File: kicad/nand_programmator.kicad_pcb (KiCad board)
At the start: 2 copper layers, 48 x 41 mm, 42 parts, among them J1 Conn_01x04, J2 Conn_01x03, J3 Conn_02x12_Odd_Even_Left, J4 Conn_02x12_Odd_Even_Right, J5 BOOT0, J6 ~{RST}, P1 USB, U1 LM1117-3.3, U2 STM32F103VCT6, Y1 Crystal_SMD_8MHz_18pF

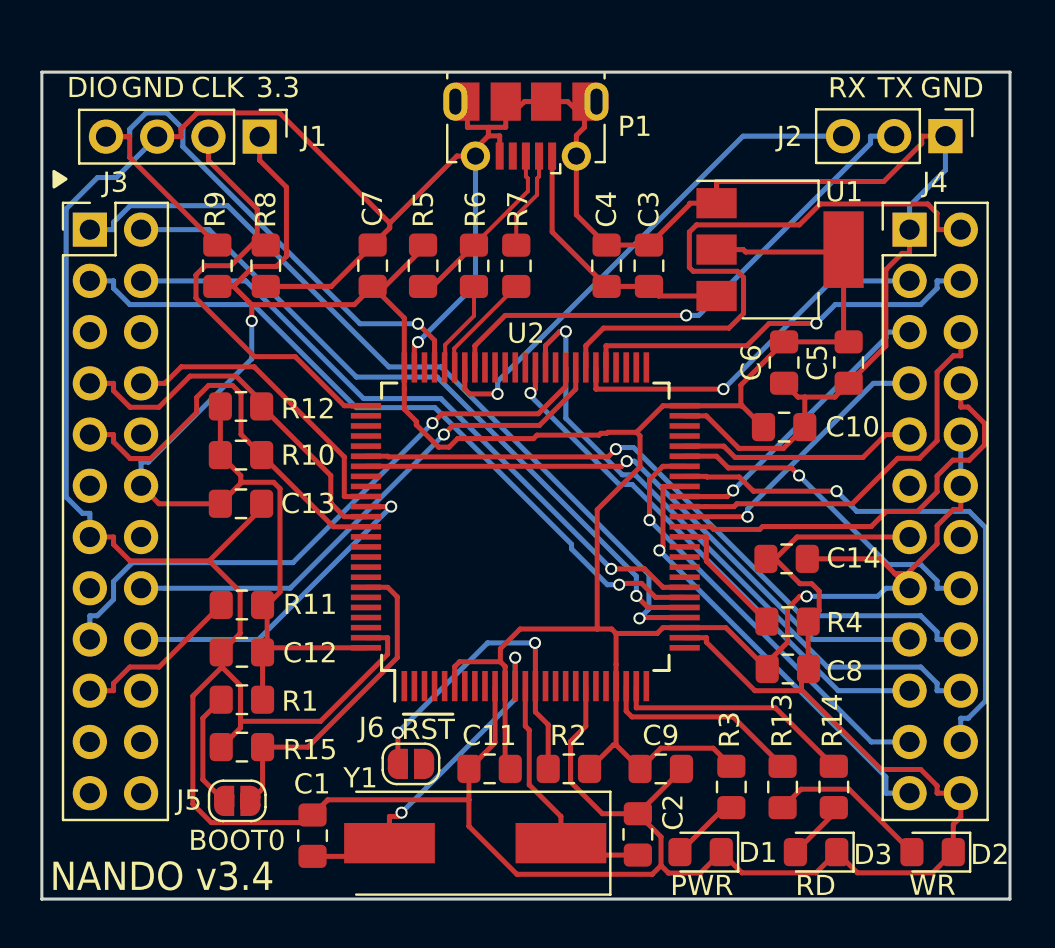
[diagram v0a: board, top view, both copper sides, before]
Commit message: Migrate mainboard and adapter_tsop48 to kicad 10 and various changes
Replace the regulator with an AMS1117-3.3 and change the USB port to a generic USB-C port.
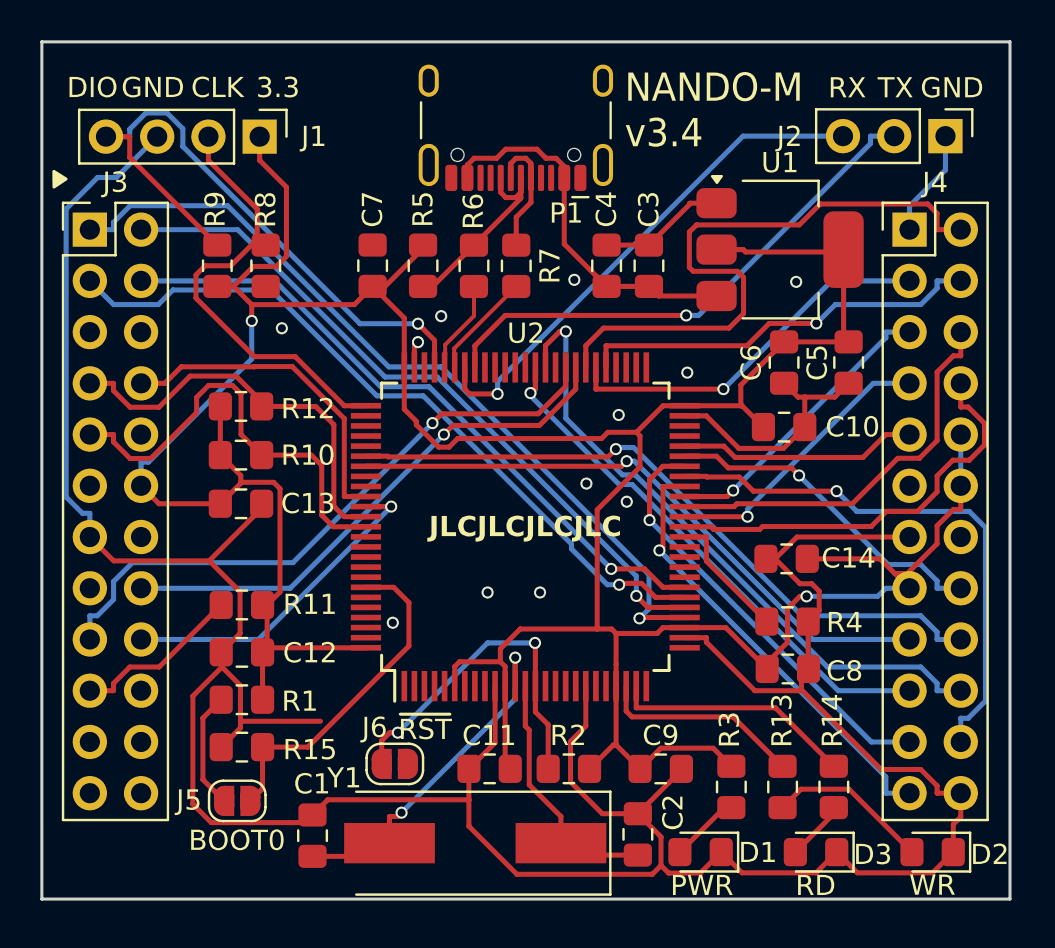
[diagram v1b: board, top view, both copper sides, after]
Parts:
- P1: value USB -> USB_C_Receptacle_USB2.0_16P; footprint lib_fp:USB_Micro-B_Molex-105017-0001 -> Connector_USB:USB_C_Receptacle_HCTL_HC-TYPE-C-16P-01A
- U1: value LM1117-3.3 -> AMS1117-3.3; footprint lib_fp:SOT-223 -> Package_TO_SOT_SMD:SOT-223-3_TabPin2
- Y1: value Crystal_SMD_8MHz_18pF -> 8MHz 18pF
- moved P1 1.30 mm to (191.4, 46.1)
- moved J6 0.80 mm to (185.4, 78.9)
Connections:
- J3 pad 10: Net-(J3-Pad10) -> unconnected-(J3-Pin_10-Pad10)
- J3 pad 11: Net-(J3-Pad11) -> unconnected-(J3-Pin_11-Pad11)
- J3 pad 14: Net-(J3-Pad14) -> unconnected-(J3-Pin_14-Pad14)
- J3 pad 15: Net-(J3-Pad15) -> unconnected-(J3-Pin_15-Pad15)
- J3 pad 20: Net-(J3-Pad20) -> unconnected-(J3-Pin_20-Pad20)
- J3 pad 21: Net-(J3-Pad21) -> unconnected-(J3-Pin_21-Pad21)
- J3 pad 22: Net-(J3-Pad22) -> unconnected-(J3-Pin_22-Pad22)
- J3 pad 23: Net-(J3-Pad23) -> unconnected-(J3-Pin_23-Pad23)
- J3 pad 24: Net-(J3-Pad24) -> unconnected-(J3-Pin_24-Pad24)
- J3 pad 5: Net-(J3-Pad5) -> unconnected-(J3-Pin_5-Pad5)
- J3 pad 6: Net-(J3-Pad6) -> unconnected-(J3-Pin_6-Pad6)
- J4 pad 35: Net-(J4-Pad35) -> unconnected-(J4-Pin_35-Pad35)
- J4 pad 38: Net-(J4-Pad38) -> unconnected-(J4-Pin_38-Pad38)
- U2 pad 1: Net-(U2-Pad1) -> unconnected-(U2-PE2/FSMC_A23/SYS_TRACECLK-Pad1)
- U2 pad 15: Net-(U2-Pad15) -> unconnected-(U2-ADC1_IN10/ADC2_IN10/ADC3_IN10/PC0-Pad15)
- U2 pad 16: Net-(U2-Pad16) -> unconnected-(U2-ADC1_IN11/ADC2_IN11/ADC3_IN11/PC1-Pad16)
- U2 pad 17: Net-(U2-Pad17) -> unconnected-(U2-ADC1_IN12/ADC2_IN12/ADC3_IN12/PC2-Pad17)
- U2 pad 18: Net-(U2-Pad18) -> unconnected-(U2-ADC1_IN13/ADC2_IN13/ADC3_IN13/PC3-Pad18)
- U2 pad 2: Net-(U2-Pad2) -> unconnected-(U2-PE3/FSMC_A19/SYS_TRACED0-Pad2)
- U2 pad 20: Net-(U2-Pad20) -> unconnected-(U2-VREF--Pad20)
- U2 pad 21: Net-(U2-Pad21) -> unconnected-(U2-VREF+-Pad21)
- U2 pad 25: Net-(U2-Pad25) -> unconnected-(U2-ADC1_IN2/ADC2_IN2/ADC3_IN2/TIM2_CH3/TIM5_CH3/USART2_TX/PA2-Pad25)
- U2 pad 26: Net-(U2-Pad26) -> unconnected-(U2-ADC1_IN3/ADC2_IN3/ADC3_IN3/TIM2_CH4/TIM5_CH4/USART2_RX/PA3-Pad26)
- U2 pad 3: Net-(U2-Pad3) -> unconnected-(U2-PE4/FSMC_A20/SYS_TRACED1-Pad3)
- U2 pad 33: Net-(U2-Pad33) -> unconnected-(U2-ADC1_IN14/ADC2_IN14/PC4-Pad33)
- U2 pad 34: Net-(U2-Pad34) -> unconnected-(U2-ADC1_IN15/ADC2_IN15/PC5-Pad34)
- U2 pad 35: Net-(U2-Pad35) -> unconnected-(U2-ADC1_IN8/ADC2_IN8/TIM1_CH2N/TIM3_CH3/TIM8_CH2N/PB0-Pad35)
- U2 pad 36: Net-(U2-Pad36) -> unconnected-(U2-ADC1_IN9/ADC2_IN9/TIM1_CH3N/TIM3_CH4/TIM8_CH3N/PB1-Pad36)
- U2 pad 4: Net-(U2-Pad4) -> unconnected-(U2-PE5/FSMC_A21/SYS_TRACED2-Pad4)
- U2 pad 47: Net-(U2-Pad47) -> unconnected-(U2-I2C2_SCL/TIM2_CH3/USART3_TX/PB10-Pad47)
- U2 pad 48: Net-(U2-Pad48) -> unconnected-(U2-ADC1_EXTI11/ADC2_EXTI11/I2C2_SDA/TIM2_CH4/USART3_RX/PB11-Pad48)
- U2 pad 5: Net-(U2-Pad5) -> unconnected-(U2-PE6/FSMC_A22/SYS_TRACED3-Pad5)
- U2 pad 51: Net-(U2-Pad51) -> unconnected-(U2-I2C2_SMBA/I2S2_WS/SPI2_NSS/TIM1_BKIN/USART3_CK/PB12-Pad51)
- U2 pad 52: Net-(U2-Pad52) -> unconnected-(U2-I2S2_CK/SPI2_SCK/TIM1_CH1N/USART3_CTS/PB13-Pad52)
- U2 pad 53: Net-(U2-Pad53) -> unconnected-(U2-SPI2_MISO/TIM1_CH2N/USART3_RTS/PB14-Pad53)
- U2 pad 54: Net-(U2-Pad54) -> unconnected-(U2-ADC1_EXTI15/ADC2_EXTI15/I2S2_SD/SPI2_MOSI/TIM1_CH3N/PB15-Pad54)
- U2 pad 60: Net-(U2-Pad60) -> unconnected-(U2-PD13/FSMC_A18/TIM4_CH2-Pad60)
- U2 pad 63: Net-(U2-Pad63) -> unconnected-(U2-I2S2_MCK/SDIO_D6/TIM3_CH1/TIM8_CH1/PC6-Pad63)
- U2 pad 64: Net-(U2-Pad64) -> unconnected-(U2-I2S3_MCK/SDIO_D7/TIM3_CH2/TIM8_CH2/PC7-Pad64)
- U2 pad 65: Net-(U2-Pad65) -> unconnected-(U2-SDIO_D0/TIM3_CH3/TIM8_CH3/PC8-Pad65)
- U2 pad 66: Net-(U2-Pad66) -> unconnected-(U2-DAC_EXTI9/SDIO_D1/TIM3_CH4/TIM8_CH4/PC9-Pad66)
- U2 pad 67: Net-(U2-Pad67) -> unconnected-(U2-RCC_MCO/TIM1_CH1/USART1_CK/PA8-Pad67)
- U2 pad 7: Net-(U2-Pad7) -> unconnected-(U2-RTC_OUT/RTC_TAMPER/PC13-Pad7)
- U2 pad 73: Net-(U2-Pad73) -> unconnected-(U2-NC-Pad73)
- U2 pad 77: Net-(U2-Pad77) -> unconnected-(U2-ADC1_EXTI15/ADC2_EXTI15/I2S3_WS/SPI1_NSS/SPI3_NSS/SYS_JTDI/TIM2_CH1/TIM2_ETR/PA15-Pad77)
- U2 pad 78: Net-(U2-Pad78) -> unconnected-(U2-SDIO_D2/UART4_TX/USART3_TX/PC10-Pad78)
- U2 pad 79: Net-(U2-Pad79) -> unconnected-(U2-ADC1_EXTI11/ADC2_EXTI11/SDIO_D3/UART4_RX/USART3_RX/PC11-Pad79)
- U2 pad 8: Net-(U2-Pad8) -> unconnected-(U2-RCC_OSC32_IN/PC14-Pad8)
- U2 pad 80: Net-(U2-Pad80) -> unconnected-(U2-SDIO_CK/UART5_TX/USART3_CK/PC12-Pad80)
- U2 pad 83: Net-(U2-Pad83) -> unconnected-(U2-PD2/SDIO_CMD/TIM3_ETR/UART5_RX-Pad83)
- U2 pad 84: Net-(U2-Pad84) -> unconnected-(U2-PD3/FSMC_CLK/USART2_CTS-Pad84)
- U2 pad 89: Net-(U2-Pad89) -> unconnected-(U2-I2S3_CK/SPI1_SCK/SPI3_SCK/SYS_JTDO-TRACESWO/TIM2_CH2/PB3-Pad89)
- U2 pad 9: Net-(U2-Pad9) -> unconnected-(U2-ADC1_EXTI15/ADC2_EXTI15/RCC_OSC32_OUT/PC15-Pad9)
- U2 pad 90: Net-(U2-Pad90) -> unconnected-(U2-SPI1_MISO/SPI3_MISO/SYS_NJTRST/TIM3_CH1/PB4-Pad90)
- U2 pad 91: Net-(U2-Pad91) -> unconnected-(U2-I2C1_SMBA/I2S3_SD/SPI1_MOSI/SPI3_MOSI/TIM3_CH2/PB5-Pad91)
- U2 pad 92: Net-(U2-Pad92) -> unconnected-(U2-I2C1_SCL/TIM4_CH1/USART1_TX/PB6-Pad92)
- U2 pad 93: Net-(U2-Pad93) -> unconnected-(U2-FSMC_NL/I2C1_SDA/TIM4_CH2/USART1_RX/PB7-Pad93)
- U2 pad 95: Net-(U2-Pad95) -> unconnected-(U2-CAN_RX/I2C1_SCL/SDIO_D4/TIM4_CH3/PB8-Pad95)
- U2 pad 96: Net-(U2-Pad96) -> unconnected-(U2-CAN_TX/DAC_EXTI9/I2C1_SDA/SDIO_D5/TIM4_CH4/PB9-Pad96)
- U2 pad 97: Net-(U2-Pad97) -> unconnected-(U2-PE0/FSMC_NBL0/TIM4_ETR-Pad97)
- U2 pad 98: Net-(U2-Pad98) -> unconnected-(U2-PE1/FSMC_NBL1-Pad98)
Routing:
- net GNDD: track 270.6 -> 181.8 mm, vias 1 -> 12
- net +5V: track 13.2 -> 18.6 mm
- net /FSMC_NWAIT: track 18.9 -> 20.4 mm
- net /FSMC_NCE2: track 20.4 -> 21.9 mm
- net /USB_N: track 4.89 -> 6.29 mm
- net /USB_P: track 8.94 -> 10.3 mm
- net /FSMC_NOE: track 15.3 -> 16.4 mm
- net /BOOT0: track 16.2 -> 16.8 mm
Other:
- board size 48 x 41 mm -> 48 x 42.5 mm
- rule pad_to_mask_clearance: 0.2 -> 0
- board text added: "JLCJLCJLCJLC"
- board text added: "NANDO-M v3.4"
- board text removed: "NANDO v3.4"

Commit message: Add LCSC part number metadata through kicad-jlcpcb-tools
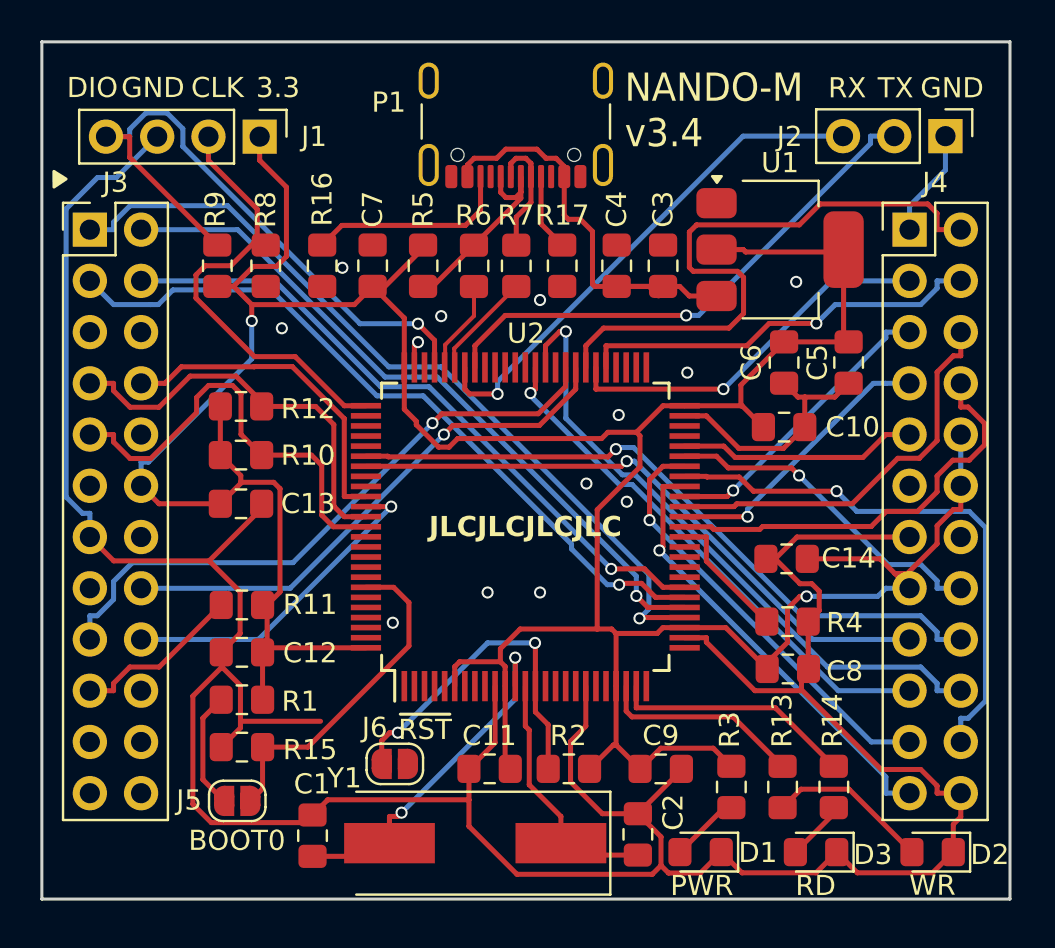
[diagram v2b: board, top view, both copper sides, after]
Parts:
- added R16: 5.1k, lib_fp:R_0805_2012Metric_Pad1.15x1.40mm_HandSolder, F.Cu at (181.8, 54.2)
- added R17: 5.1k, lib_fp:R_0805_2012Metric_Pad1.15x1.40mm_HandSolder, F.Cu at (193.7, 54.2)
- P1: footprint Connector_USB:USB_C_Receptacle_HCTL_HC-TYPE-C-16P-01A -> Connector_USB:USB_C_Receptacle_GCT_USB4105-xx-A_16P_TopMnt_Horizontal
- moved C3 0.70 mm to (198.7, 54.2)
- moved C4 0.50 mm to (196.4, 54.2)
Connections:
- P1 pad A5: unconnected-(P1-CC1-PadA5) -> Net-(P1-CC1)
- P1 pad B5: unconnected-(P1-CC2-PadB5) -> Net-(P1-CC2)
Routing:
- net Net-(P1-CC2): track 0.00 -> 10.2 mm
- net GNDD: track 181.8 -> 173.5 mm, vias 12 -> 13
- net Net-(P1-CC1): track 0.00 -> 3.76 mm
- net +5V: track 18.6 -> 22.1 mm
- net +3V3: track 179.4 -> 177.2 mm
- net Net-(U2-RCC_OSC_IN): track 17.5 -> 16.6 mm
- net Net-(U2-RCC_OSC_OUT): track 12.6 -> 11.7 mm
- net /USB_DN: track 5.30 -> 4.65 mm
- net /USB_DP: track 4.62 -> 3.97 mm
- net /SWCLK: track 22.2 -> 21.6 mm
